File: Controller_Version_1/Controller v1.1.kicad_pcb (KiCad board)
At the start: 2 copper layers, 97 parts, among them sw1 5.1mm switch

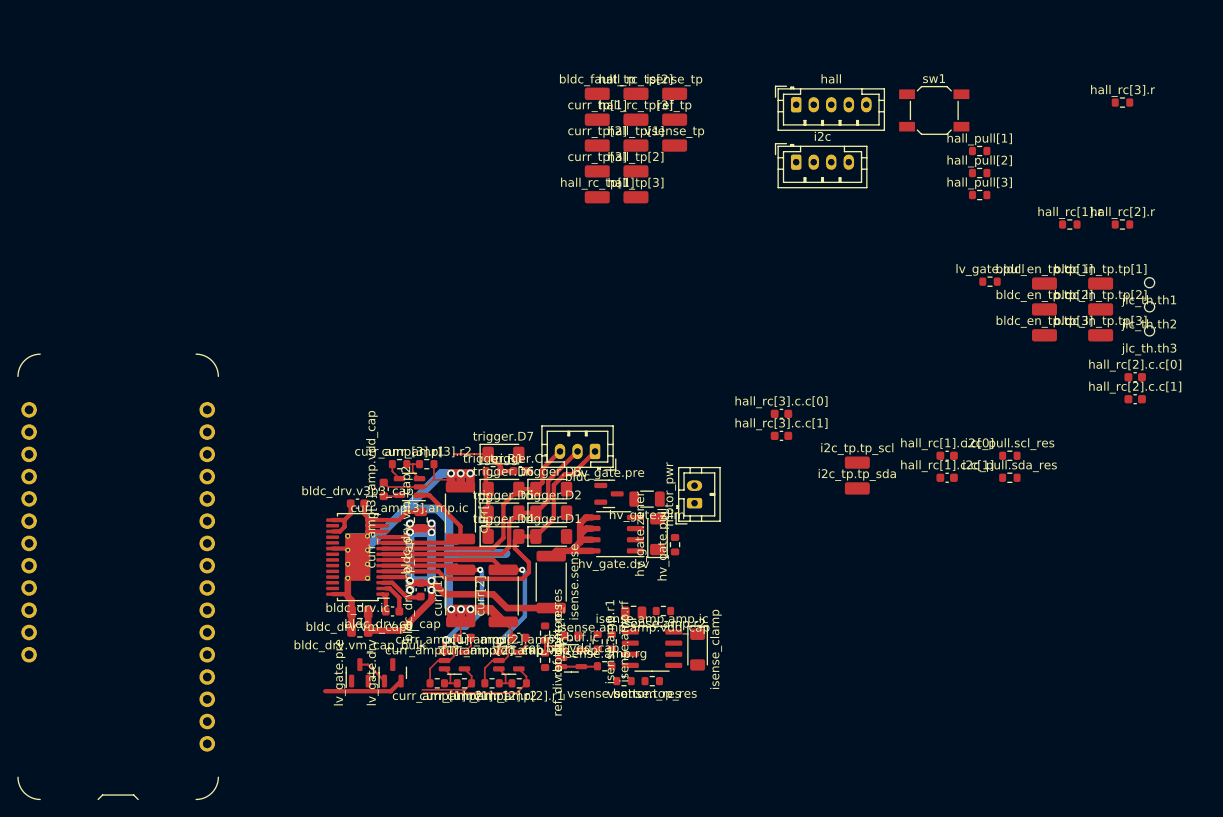
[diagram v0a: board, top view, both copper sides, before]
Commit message: [PCB] Update preliminary version of board layout, to be improved
    Density
    Clean power traces
    (potentially) Smaller diodes
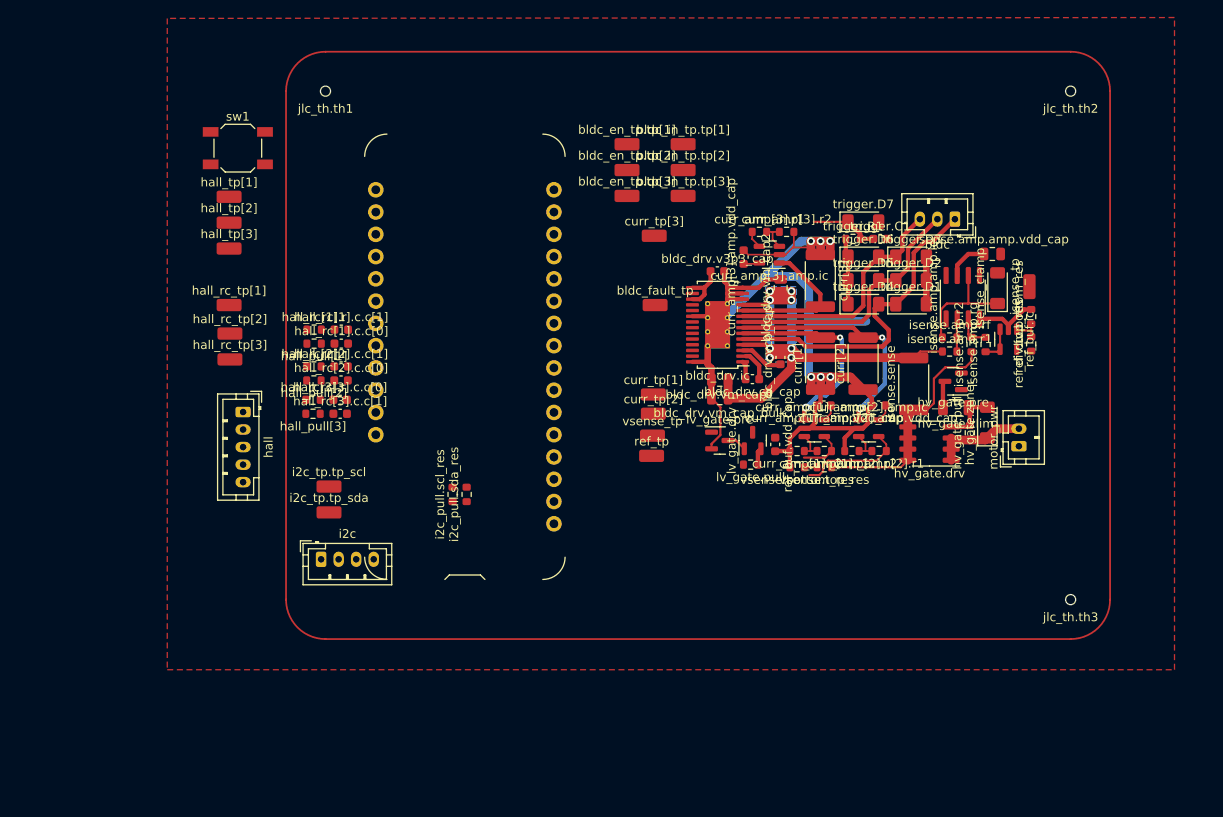
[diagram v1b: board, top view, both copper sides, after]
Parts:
- moved hall_rc[3].r 98.4 mm to (68.1, 111.7)
- moved jlc_th.th1 96.5 mm to (69.5, 76.5)
- moved hall_rc[2].r 93.7 mm to (68.2, 107.9)
- moved hall_rc[2].c.c[1] 90.7 mm to (71.3, 107.9)
- moved hall_rc[2].c.c[0] 90.6 mm to (71.3, 109.5)
- moved hall_rc[1].r 87.0 mm to (68.2, 103.7)
- moved hall_pull[3] 80.0 mm to (68.1, 113.3), turned to 180 degrees
- moved sw1 79.6 mm to (59.5, 83.0)
- moved hall_pull[2] 79.5 mm to (68.2, 109.5), turned to 180 degrees
- moved hall_pull[1] 79.0 mm to (68.2, 105.3), turned to 180 degrees
- moved hall 72.2 mm to (60.1, 113.1), turned to -90 degrees
- moved hall_rc[1].c.c[1] 71.2 mm to (71.3, 103.7)
- moved i2c 70.6 mm to (69.0, 129.9)
- moved hall_rc[1].c.c[0] 70.3 mm to (71.3, 105.3)
- moved ref_div.bottom_res 67.9 mm to (150.1, 102.2), turned to 90 degrees
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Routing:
- net gnd: track 117.4 -> 146.2 mm
- net hv_gate.output: track 13.2 -> 31.4 mm
- net isense.out: track 0.00 -> 13.2 mm
- net motor_pwr.pwr: track 0.00 -> 10.9 mm
- net mcu.pwr_out: track 9.13 -> 1.96 mm
- net hv_gate.pull.b: track 0.00 -> 6.44 mm
- net isense.amp.r2.b: track 0.00 -> 3.85 mm
- net isense.amp.r1.b: track 0.00 -> 3.74 mm
- net isense.pwr_out: track 63.2 -> 66.8 mm
- net hv_gate.pre.drain: track 0.00 -> 3.09 mm
- net curr_amp[1].output: track 7.93 -> 5.45 mm
- net curr_amp[2].output: track 14.2 -> 12.3 mm
- net vsense.output: track 0.00 -> 1.45 mm
- net lv_gate.pre.drain: track 3.58 -> 2.25 mm
- added copper zone on F.Cu, net gnd
- added copper zone on B.Cu, net isense.pwr_out

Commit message: Changed pin assignments
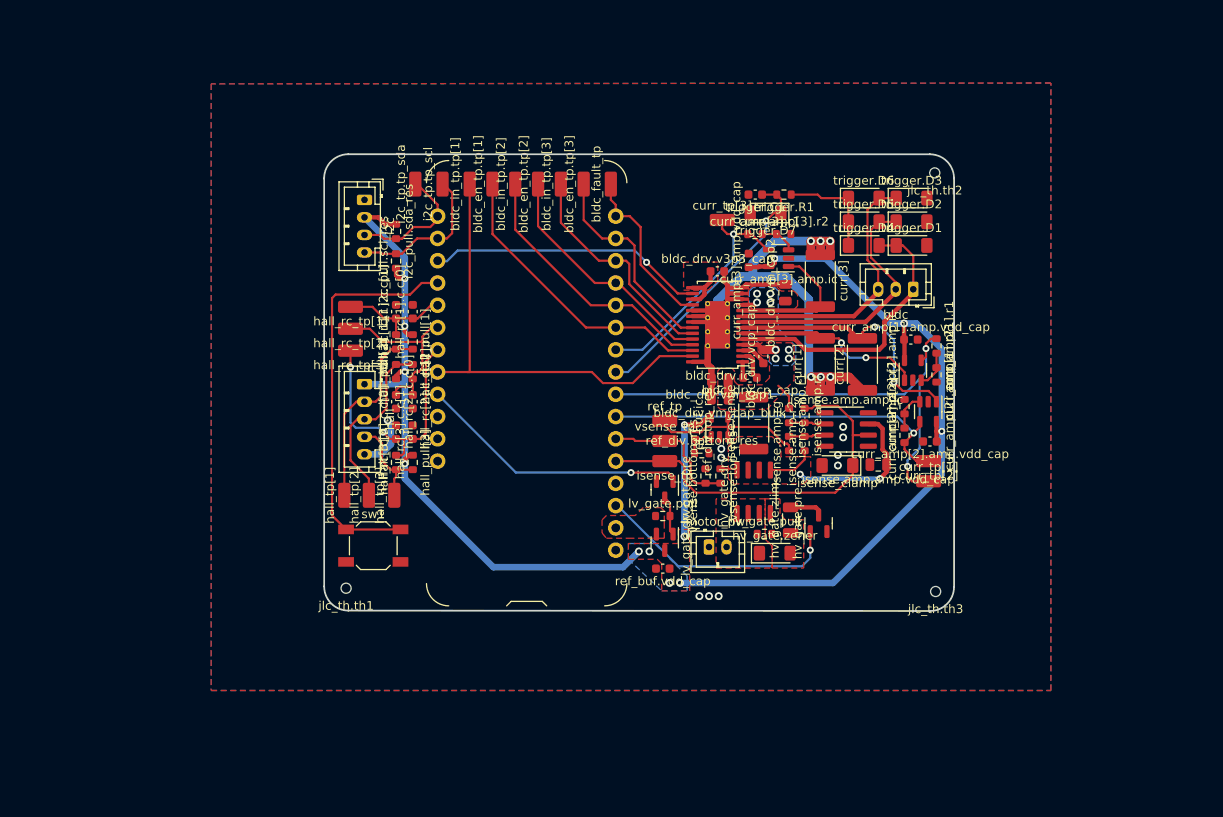
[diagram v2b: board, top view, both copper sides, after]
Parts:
- moved jlc_th.th1 56.7 mm to (71.9, 133.2)
- moved sw1 47.9 mm to (75.0, 128.3)
- moved isense_tp 46.1 mm to (108.2, 118.7), turned to 180 degrees
- moved i2c 41.3 mm to (74.0, 88.9), turned to -90 degrees
- moved ref_div.bottom_res 40.7 mm to (112.5, 117.8), turned to 0 degrees
- moved ref_div.top_res 39.6 mm to (111.7, 115.4), turned to -90 degrees
- moved i2c_tp.tp_sda 38.7 mm to (79.8, 87.1), turned to 90 degrees
- moved motor_pwr 37.2 mm to (113.3, 128.5), turned to 0 degrees
- moved i2c_tp.tp_scl 36.9 mm to (82.9, 87.1), turned to 90 degrees
- moved hall_tp[1] 36.5 mm to (71.7, 122.6), turned to 90 degrees
- moved hall_tp[2] 35.0 mm to (74.5, 122.6), turned to 90 degrees
- moved ref_buf.ic 34.4 mm to (114.5, 114.8), turned to 90 degrees
- moved hall_tp[3] 33.9 mm to (77.4, 122.6), turned to 90 degrees
- moved curr_tp[1] 32.9 mm to (138.3, 121.0)
- moved curr_tp[2] 31.9 mm to (138.3, 118.7), turned to 180 degrees
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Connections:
- mcu pad 10: curr_amp[1].output -> curr_amp[3].output
- mcu pad 11: mcu.gpio.bldc_in_1 -> mcu.gpio.bldc_en_1
- mcu pad 12: mcu.gpio.bldc_en_1 -> mcu.gpio.bldc_in_2
- mcu pad 13: mcu.gpio.bldc_in_2 -> mcu.gpio.bldc_en_2
- mcu pad 14: mcu.gpio.bldc_en_2 -> mcu.gpio.bldc_in_3
- mcu pad 15: mcu.gpio.bldc_in_3 -> mcu.gpio.bldc_en_3
- mcu pad 16: lv_gate.control -> bldc_drv.nfault
- mcu pad 17: mcu.gpio.bldc_en_3 -> i2c_pull.i2c.sda
- mcu pad 18: bldc_drv.nreset -> i2c_pull.i2c.scl
- mcu pad 19: bldc_drv.nfault -> bldc_drv.nreset
- mcu pad 21: i2c_pull.i2c.sda -> hall_rc[1].output
- mcu pad 22: i2c_pull.i2c.scl -> hall_rc[2].output
- mcu pad 23: hall_rc[1].output -> hall_rc[3].output
- mcu pad 24: hall_rc[2].output -> mcu.gpio.bldc_in_1
- mcu pad 25: hall_rc[3].output -> lv_gate.control
- mcu pad 3: trigger.trigger_out -> hv_gate.control
- mcu pad 7: hv_gate.control -> curr_amp[2].output
- mcu pad 8: curr_amp[3].output -> curr_amp[1].output
- mcu pad 9: curr_amp[2].output -> trigger.trigger_out
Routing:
- net lv_gate.output: track 5.77 -> 178.5 mm, vias 0 -> 13
- net isense.pwr_out: track 66.8 -> 10.9 mm
- net gnd: track 146.2 -> 93.6 mm, vias 6 -> 16
- net mcu.gpio.bldc_in_1: track 0.00 -> 52.6 mm
- net curr_amp[1].output: track 5.45 -> 57.1 mm, vias 0 -> 2
- net sw1.out: track 0.00 -> 46.0 mm
- net mcu.gpio.bldc_en_1: track 0.00 -> 34.0 mm
- net bldc_drv.nreset: track 0.00 -> 31.6 mm, vias 0 -> 1
- net isense.out: track 13.2 -> 44.6 mm
- net lv_gate.control: track 0.00 -> 31.3 mm, vias 0 -> 1
- net mcu.gpio.bldc_in_2: track 0.00 -> 30.8 mm
- net hall_rc[3].output: track 0.00 -> 30.5 mm, vias 0 -> 2
- net curr_amp[2].output: track 12.3 -> 42.0 mm, vias 0 -> 1
- net hv_gate.control: track 0.00 -> 28.5 mm, vias 0 -> 1
- net mcu.gpio.bldc_en_2: track 0.00 -> 27.7 mm
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- added copper zone on F.Cu, net bldc_drv.ic.v3p3
- added copper zone on B.Cu, net gnd
- added copper zone on F.Cu, net hv_gate.output
- added copper zone on F.Cu, net hv_gate.pull.b
- added copper zone on F.Cu, net isense.pwr_out
- added copper zone on B.Cu, net lv_gate.output
- added copper zone on F.Cu, net lv_gate.output
- added copper zone on F.Cu, net mcu.pwr_out
- added copper zone on F.Cu, net motor_pwr.pwr
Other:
- board outline added: 71.9 x 52.1 mm

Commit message: Update Controller v1.1.kicad_pcb
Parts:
- moved jlc_th.th2 1.30 mm to (140.4, 85.8)
- moved jlc_th.th3 1.30 mm to (140.4, 133.6)
- moved jlc_th.th1 1.25 mm to (70.7, 133.2)
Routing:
- net lv_gate.output: track 178.5 -> 174.1 mm
- net gnd: track 93.6 -> 91.9 mm, vias 16 -> 23
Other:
- board size 71.9 x 52.1 mm -> 74.5 x 52.1 mm
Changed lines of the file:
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@@
   )
   (footprint "edg:JlcToolingHole_1.152mm" (layer "F.Cu")
-    (at 139.050001 85.825001)
+    (at 140.350001 85.825001)
     (descr "Tooling holes for JLC assembly, 1.152 mm hole + 1.3mm soldermask opening")
     (property "Sheetfile" "edg.BoardTop.JlcToolingHoles")
@@
   )
   (footprint "edg:JlcToolingHole_1.152mm" (layer "F.Cu")
-    (at 71.9 133.2)
+    (at 70.65 133.2)
     (descr "Tooling holes for JLC assembly, 1.152 mm hole + 1.3mm soldermask opening")
     (property "Sheetfile" "edg.BoardTop.JlcToolingHoles")
@@
   )
   (footprint "edg:JlcToolingHole_1.152mm" (layer "F.Cu")
-    (at 139.15 133.575)
+    (at 140.45 133.575)
     (descr "Tooling holes for JLC assembly, 1.152 mm hole + 1.3mm soldermask opening")
     (property "Sheetfile" "edg.BoardTop.JlcToolingHoles")
@@
   (gr_arc (start 137.2 128.873143) (mid 136.699889 128.562075) (end 136.7 127.973143)
     (stroke (width 0.5) (type default)) (layer "F.Mask"))
-  (gr_arc (start 138.5 83.7) (mid 140.444544 84.505456) (end 141.25 86.45)
+  (gr_arc (start 139.9 83.7) (mid 141.844544 84.505456) (end 142.65 86.45)
     (stroke (width 0.2) (type default)) (layer "Edge.Cuts"))
-  (gr_arc (start 72.15 135.75) (mid 70.205456 134.944544) (end 69.4 133)
+  (gr_arc (start 70.9 135.75) (mid 68.955456 134.944544) (end 68.15 133)
     (stroke (width 0.2) (type default)) (layer "Edge.Cuts"))
-  (gr_line (start 69.394544 86.444544) (end 69.4 133)
+  (gr_line (start 68.144544 86.444544) (end 68.15 133)
     (stroke (width 0.2) (type default)) (layer "Edge.Cuts"))
-  (gr_line (start 72.15 135.75) (end 138.5 135.8)
+  (gr_line (start 70.9 135.75) (end 139.9 135.8)
     (stroke (width 0.2) (type default)) (layer "Edge.Cuts"))
-  (gr_arc (start 69.394544 86.444544) (mid 70.2 84.5) (end 72.144544 83.694544)
+  (gr_arc (start 68.144544 86.444544) (mid 68.949999 84.499999) (end 70.894544 83.694544)
     (stroke (width 0.2) (type default)) (layer "Edge.Cuts"))
-  (gr_line (start 72.144544 83.694544) (end 138.5 83.7)
+  (gr_line (start 70.894544 83.694544) (end 139.9 83.7)
     (stroke (width 0.2) (type default)) (layer "Edge.Cuts"))
-  (gr_line (start 141.25 86.45) (end 141.25 133.05)
+  (gr_line (start 142.65 86.45) (end 142.65 133.05)
     (stroke (width 0.2) (type default)) (layer "Edge.Cuts"))
-  (gr_arc (start 141.25 133.05) (mid 140.444544 134.994544) (end 138.5 135.8)
+  (gr_arc (start 142.65 133.05) (mid 141.844544 134.994544) (end 139.9 135.8)
     (stroke (width 0.2) (type default)) (layer "Edge.Cuts"))
   (segment (start 137.5 107.2) (end 137.65 107.2) (width 0.25) (layer "F.Cu") (net 1))
@@
   (segment (start 124.9875 110.5375) (end 124.95 110.5) (width 1) (layer "F.Cu") (net 24))
   (segment (start 126.05 109.1) (end 126.05 110.5125) (width 1) (layer "F.Cu") (net 24))
-  (segment (start 111.4125 102.825) (end 113.15 102.825) (width 0.5) (layer "F.Cu") (net 24))
   (segment (start 115.4 99.575) (end 115.4 98.925) (width 0.5) (layer "F.Cu") (net 24))
   (segment (start 124.95 109.1) (end 126.05 109.1) (width 1) (layer "F.Cu") (net 24))
@@
   (segment (start 129.275 109.1) (end 130.8 110.625) (width 1) (layer "F.Cu") (net 24))
   (via (at 128.6 114.8) (size 0.9) (drill 0.5) (layers "F.Cu" "B.Cu") (net 24))
+  (via (at 129.8 96.8) (size 0.9) (drill 0.5) (layers "F.Cu" "B.Cu") (net 24))
   (via (at 127.15 109.1) (size 0.9) (drill 0.5) (layers "F.Cu" "B.Cu") (net 24))
+  (via (at 76.2 100.9) (size 0.9) (drill 0.5) (layers "F.Cu" "B.Cu") (net 24))
   (via (at 126.025 93.60625) (size 0.9) (drill 0.5) (layers "F.Cu" "B.Cu") (net 24))
+  (via (at 113.6 88.3) (size 0.9) (drill 0.5) (layers "F.Cu" "B.Cu") (net 24))
+  (via (at 114.7 88.3) (size 0.9) (drill 0.5) (layers "F.Cu" "B.Cu") (net 24))
   (via (at 114.7 118.3) (size 0.9) (drill 0.5) (layers "F.Cu" "B.Cu") (net 24))
   (via (at 128 118) (size 0.9) (drill 0.5) (layers "F.Cu" "B.Cu") (net 24))
+  (via (at 130.6 97.6) (size 0.9) (drill 0.5) (layers "F.Cu" "B.Cu") (net 24))
   (via (at 128.6 116) (size 0.9) (drill 0.5) (layers "F.Cu" "B.Cu") (net 24))
+  (via (at 129 96) (size 0.9) (drill 0.5) (layers "F.Cu" "B.Cu") (net 24))
+  (via (at 115.8 88.3) (size 0.9) (drill 0.5) (layers "F.Cu" "B.Cu") (net 24))
   (via (at 113.3 134.1) (size 0.9) (drill 0.5) (layers "F.Cu" "B.Cu") (net 24))
   (via (at 114.7 117.3) (size 0.9) (drill 0.5) (layers "F.Cu" "B.Cu") (net 24))
@@
   (via (at 135.55 103) (size 0.9) (drill 0.5) (layers "F.Cu" "B.Cu") (net 37))
   (via (at 78.6 119) (size 0.8) (drill 0.4) (layers "F.Cu" "B.Cu") (net 37))
-  (via (at 110.5 127.3) (size 0.9) (drill 0.5) (layers "F.Cu" "B.Cu") (net 37))
+  (via (at 110.5 122.9) (size 0.9) (drill 0.5) (layers "F.Cu" "B.Cu") (net 37))
   (via (at 108.8 132.6) (size 0.9) (drill 0.5) (layers "F.Cu" "B.Cu") (net 37))
   (via (at 120.8 95.6) (size 0.8) (drill 0.4) (layers "F.Cu" "B.Cu") (net 37))
@@
   (segment (start 78.6 103.7) (end 78.6 95.5) (width 0.75) (layer "B.Cu") (net 37))
   (segment (start 139.85 120.2) (end 127.45 132.6) (width 0.75) (layer "B.Cu") (net 37))
-  (segment (start 110.5 127.3) (end 110.5 114.55) (width 0.75) (layer "B.Cu") (net 37))
+  (segment (start 110.5 122.9) (end 110.5 114.55) (width 0.75) (layer "B.Cu") (net 37))
   (segment (start 78.6 109.925) (end 74 109.925) (width 0.75) (layer "B.Cu") (net 37))
   (segment (start 127.45 132.6) (end 110 132.6) (width 0.75) (layer "B.Cu") (net 37))
@@
       (pts
         (xy 115.5 117)
-        (xy 115.5 120.1)
-        (xy 115.5 120.7)
-        (xy 116.1 121.3)
-        (xy 124.1 121.3)
-        (xy 124.9 120.5)
+        (xy 115.5 118.9)
+        (xy 113.9 118.9)
+        (xy 113.9 120.1)
+        (xy 114.4 120.6)
+        (xy 115.5 120.6)
+        (xy 115.5 121.6)
+        (xy 124.1 121.6)
+        (xy 124.9 120.8)
         (xy 124.9 118.2)
         (xy 121.5 118.2)
@@
         (xy 101.6 127.5)
         (xy 104.1 127.5)
-        (xy 104.1 127.5)
         (xy 107.6 127.5)
         (xy 108.2 127.5)
@@
         (xy 111.1 133.5)
         (xy 111.1 128.1)
-        (xy 111.1 126.5)
-        (xy 109.8 126.5)
+        (xy 111.1 122.2)
+        (xy 109.8 122.2)
         (xy 109.8 128.1)
       )

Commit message: [PCB] Finished layout (need to fix duck)
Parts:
- added svg2mod: G***, edg:Symbol_DucklingSolid, F.Cu at (109.0, 87.5)
- moved is3 2.00 mm to (113.6, 92.8)
- renumbered ref_buf.vdd_cap to C1, bldc_drv.vm_cap1 to C10, bldc_drv.vm_cap2 to C11, bldc_drv.v3p3_cap to C12, bldc_drv.cp_cap to C13, bldc_drv.vcp_cap to C14, curr_amp[1].amp.vdd_cap to C15, curr_amp[2].amp.vdd_cap to C16, curr_amp[3].amp.vdd_cap to C17, trigger.C1 to C18, hall_rc[1].c.c[0] to C2, hall_rc[1].c.c[1] to C3, hall_rc[2].c.c[0] to C4, hall_rc[2].c.c[1] to C5, hall_rc[3].c.c[0] to C6, hall_rc[3].c.c[1] to C7, isense.amp.amp.vdd_cap to C8, bldc_drv.vm_cap_bulk to C9, hv_gate.zener to D1, isense_clamp to D2, trigger.D1 to D3, trigger.D2 to D4, trigger.D3 to D5, trigger.D4 to D6, trigger.D5 to D7, trigger.D6 to D8, trigger.D7 to D9, jlc_th.th1 to H1, jlc_th.th2 to H2, jlc_th.th3 to H3, motor_pwr to J1, i2c to J2, hall to J3, bldc to J4, lv_gate.pre to Q1, lv_gate.drv to Q2, hv_gate.pre to Q3, hv_gate.drv to Q4, lv_gate.pull to R1, hall_pull[3] to R10, hall_rc[3].r to R11, hv_gate.pull to R12, hv_gate.zlim to R13, vsense.top_res to R14, vsense.bottom_res to R15, isense.sense to R16, isense.amp.r1 to R17, isense.amp.r2 to R18, isense.amp.rf to R19, i2c_pull.scl_res to R2, isense.amp.rg to R20, curr[1] to R21, curr_amp[1].r1 to R22, curr_amp[1].r2 to R23, curr[2] to R24, curr_amp[2].r1 to R25, curr_amp[2].r2 to R26, curr[3] to R27, curr_amp[3].r1 to R28, curr_amp[3].r2 to R29, i2c_pull.sda_res to R3, trigger.R1 to R30, ref_div.top_res to R4, ref_div.bottom_res to R5, hall_pull[1] to R6, hall_rc[1].r to R7, hall_pull[2] to R8, hall_rc[2].r to R9, sw1 to SW1, mcu to U1, ref_buf.ic to U2, isense.amp.amp.ic to U3, bldc_drv.ic to U4, curr_amp[1].amp.ic to U5, curr_amp[2].amp.ic to U6, curr_amp[3].amp.ic to U7, bldc_en_tp.tp[1] to en1, bldc_en_tp.tp[2] to en2, bldc_en_tp.tp[3] to en3, hall_rc_tp[1] to ha1, hall_rc_tp[2] to ha2, hall_rc_tp[3] to ha3, hall_tp[1] to hp1, hall_tp[2] to hp2, hall_tp[3] to hp3, bldc_in_tp.tp[1] to in1, bldc_in_tp.tp[2] to in2, bldc_in_tp.tp[3] to in3, curr_tp[2] to is1, curr_tp[1] to is2, curr_tp[3] to is3, isense_tp to isn, bldc_fault_tp to nft, ref_tp to ref, i2c_tp.tp_scl to scl, i2c_tp.tp_sda to sda, vsense_tp to vsn
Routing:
- net lv_gate.output: track 174.1 -> 175.1 mm
- net gnd: vias 23 -> 24
